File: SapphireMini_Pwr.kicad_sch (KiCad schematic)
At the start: 34 parts, among them IC501 SLG59M1446V, J501 JST, Q501 BC857BS, Q502 SSM3J378R,LXHF

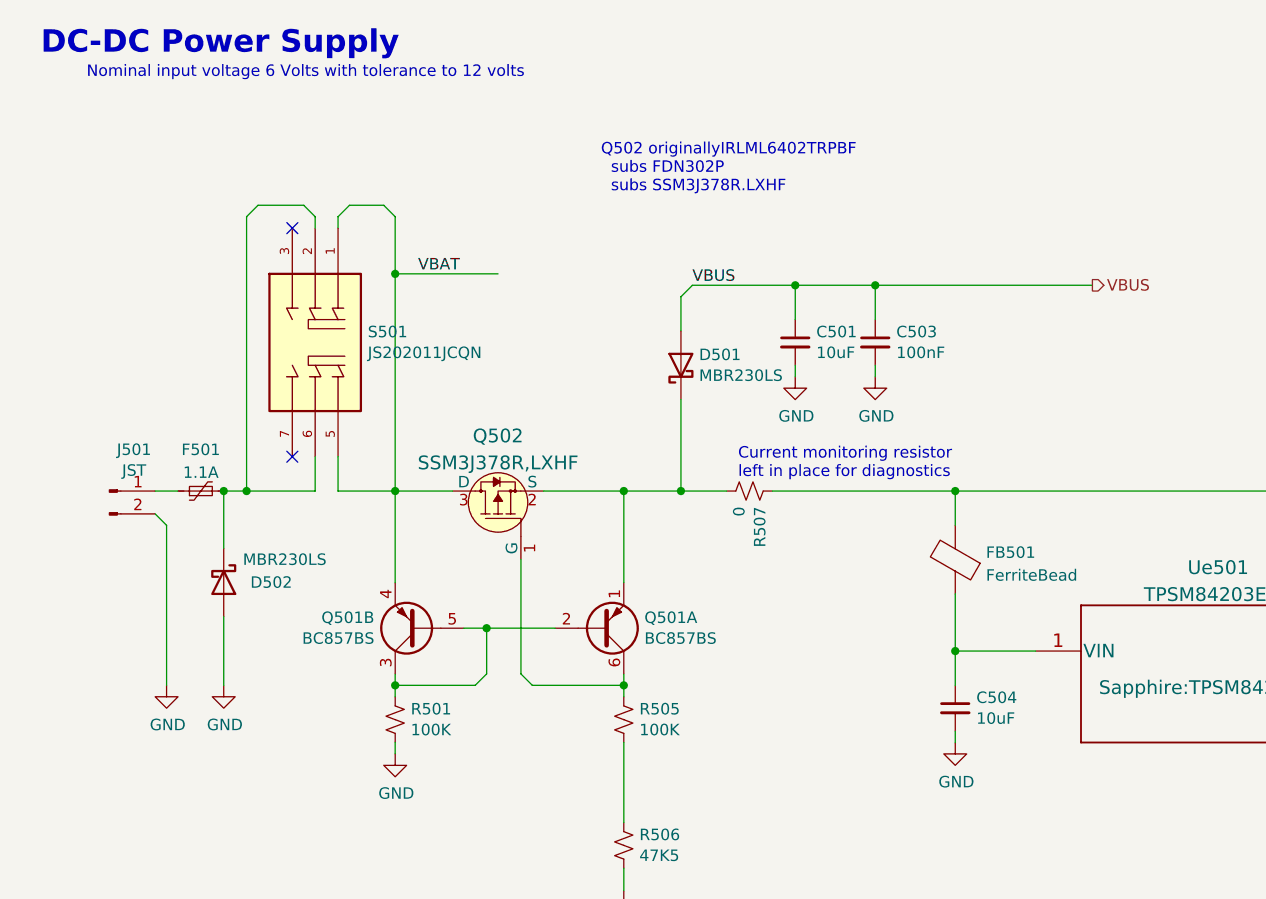
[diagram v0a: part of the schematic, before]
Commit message: Updated to fix noted problems
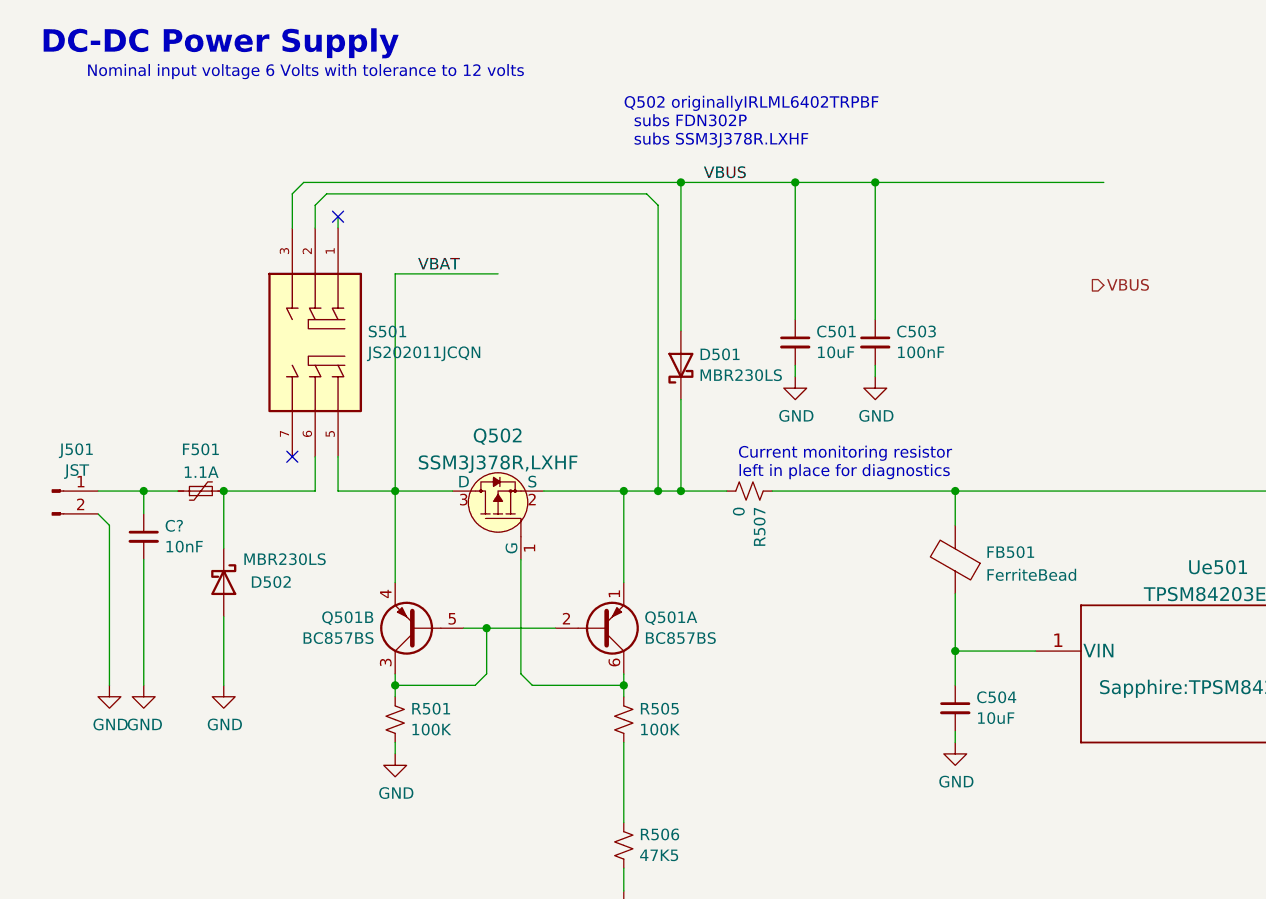
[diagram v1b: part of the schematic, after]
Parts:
- added C?: 10nF, Capacitor_SMD:C_0402_1005Metric, symbol Device:C_Small
- S501: footprint Sapphire:SW_JS202011JCQN -> Sapphire:SW_JS202011JCQN_handSolder
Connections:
- net GND: now also C?.2
- net VBAT: no longer S501.1
- net VBUS: now also S501.3
- net at F501.1, J501.1 (Pin_1): now also C?.1
- net at D501.1 (K), Q501.1 (E1), Q502.2 (S)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: now also S501.2
- net at D502.1 (K), F501.2, S501.6: no longer S501.2
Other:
- moved on the sheet: J501

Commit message: InProgress
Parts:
- gave numbers to parts that had none: 1
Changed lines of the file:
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@@
   (symbol (lib_id "power:GND") (at 29.21 86.36 0) (unit 1)
     (in_bom yes) (on_board yes)
-    (property "Reference" "#PWR?" (id 0) (at 29.21 92.71 0)
+    (property "Reference" "#PWR0113" (id 0) (at 29.21 92.71 0)
       (effects (font (size 1.27 1.27)) hide)
     )
@@
   (symbol (lib_id "Device:C_Small") (at 29.21 69.85 0) (unit 1)
     (in_bom yes) (on_board yes)
-    (property "Reference" "C?" (id 0) (at 31.5468 68.6816 0)
+    (property "Reference" "C512" (id 0) (at 31.5468 68.6816 0)
       (effects (font (size 1.27 1.27)) (justify left))
     )

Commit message: M2R2 basic DRC passed
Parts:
- C511: value FC0H224ZFTBR24 -> RSCSK2043R3D011004T; footprint CAPAE1080X880N -> Sapphire:RSCSK2043R3D01004T
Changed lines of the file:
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@@
       (effects (font (size 1.27 1.27)) (justify left))
     )
-    (property "Value" "FC0H224ZFTBR24" (id 1) (at 217.17 137.16 90)
+    (property "Value" "RSCSK2043R3D011004T" (id 1) (at 210.82 137.16 90)
       (effects (font (size 1.27 1.27)) (justify left))
     )
-    (property "Footprint" "CAPAE1080X880N" (id 2) (at 238.76 139.7 0)
+    (property "Footprint" "Sapphire:RSCSK2043R3D01004T" (id 2) (at 238.76 139.7 0)
       (effects (font (size 1.27 1.27)) (justify left) hide)
     )

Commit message: End of Weekend
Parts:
- removed C504: 10uF, Capacitor_SMD:C_1210_3225Metric, symbol Device:C_Small
- removed Ue501: TPSM84203EAB, Sapphire:TPSM84203EAB, symbol sapphireMini:TPSM84203EAB
- added C504: 390pF, Capacitor_SMD:C_0603_1608Metric, symbol Device:C
- added L501: 2.2uH, SapphineMinimal:74439344022, symbol sapphireMini:L_Core_Ferrite-Device
- added R509, R510: 100K, Resistor_SMD:R_0603_1608Metric, symbol Device:R_Small_US
- added R511: 562K, Resistor_SMD:R_0603_1608Metric, symbol Device:R_Small_US
- added R516: 180K, Resistor_SMD:R_0603_1608Metric, symbol Device:R_Small_US
- added U501: TPS62150, Package_DFN_QFN:VQFN-16-1EP_3x3mm_P0.5mm_EP1.68x1.68mm_ThermalVias, symbol Regulator_Switching:TPS62150
- C502: value 47uF -> 10uF; footprint Capacitor_SMD:C_1210_3225Metric -> Capacitor_SMD:C_0805_2012Metric; MPN CL32A476KOJNNNE -> GRM21BR61E106MA73L
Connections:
- net GND: now also C505.1, C504.2, R516.2, U501.15 (PGND), U501.16 (PGND), U501.17 (EP), U501.6 (AGND); no longer C505.2
- net P3V3: now also C505.2, L501.2, R510.1, R511.1, U501.14 (VOS), U501.7 (FSW); no longer C502.1, C505.1
- net PWR_IN: now also C502.1, R509.1, U501.10 (AVIN), U501.11 (PVIN), U501.12 (PVIN); no longer R507.2
- net at FB501.1: now also R507.2
- new net: R511.2, R516.1, U501.5 (FB)
- new net: C504.1, U501.9 (SS/TR)
- new net: R510.2, U501.4 (PG)
- new net: L501.1, U501.1 (SW), U501.2 (SW), U501.3 (SW)
- new net VBAT_EN: R509.2, U501.13 (EN)
- no-connect marks 2 -> 3
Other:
- moved on the sheet: C501, C503, C505, FB501

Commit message: Partial Routing
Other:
- note added: "L501"
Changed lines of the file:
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@@
     (stroke (width 0) (type default) (color 0 0 0 0))
+  )
+  (text "L501" (at 157.48 82.55 0)
+    (effects (font (size 1.27 1.27)) (justify left bottom))
   )
   (text "R514,515 used to set\nramp up" (at 15.24 166.37 0)

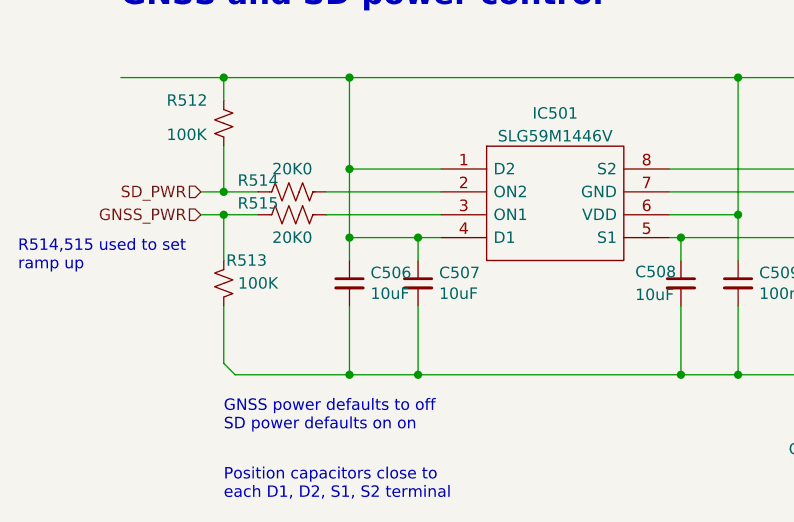
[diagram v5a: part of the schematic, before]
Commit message: Board Assembled w/ errors.  Ready for redo
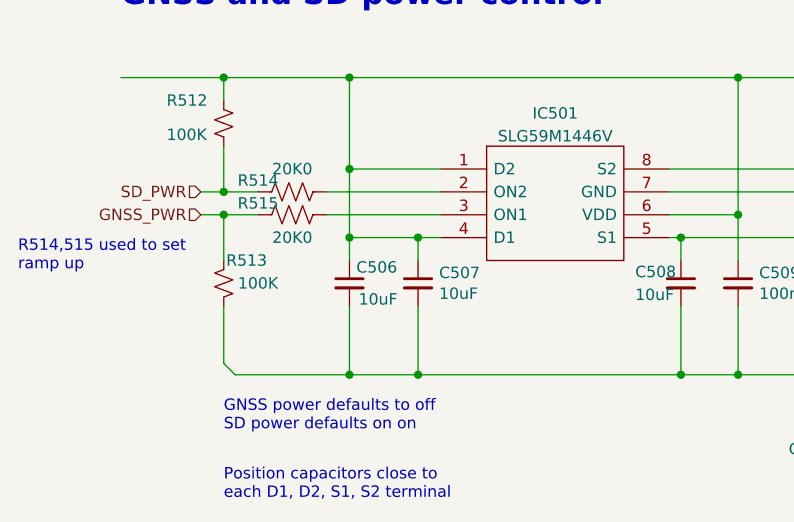
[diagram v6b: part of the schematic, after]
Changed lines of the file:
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@@
   (symbol (lib_id "Device:C_Small") (at 52.07 167.64 0) (unit 1)
     (in_bom yes) (on_board yes)
-    (property "Reference" "C506" (id 0) (at 54.4068 166.4716 0)
+    (property "Reference" "C506" (id 0) (at 52.832 165.862 0)
       (effects (font (size 1.27 1.27)) (justify left))
     )
-    (property "Value" "10uF" (id 1) (at 54.4068 168.783 0)
+    (property "Value" "10uF" (id 1) (at 53.086 169.418 0)
       (effects (font (size 1.27 1.27)) (justify left))
     )
